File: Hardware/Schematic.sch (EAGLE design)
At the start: 105 parts, among them IC1 BQ25180YBGR, IC2 DRV2605YZFR, IC3 BMA423, IC9 RT6160AWSC, J1 503480-2400, J2 TC2030-IDC, J4 KH-TYPE-C-16P, Q1 20V/4.2A/52mΩ/1.4W, Q3 SI1308EDL-T1-GE3, U1 NRF52840_QF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

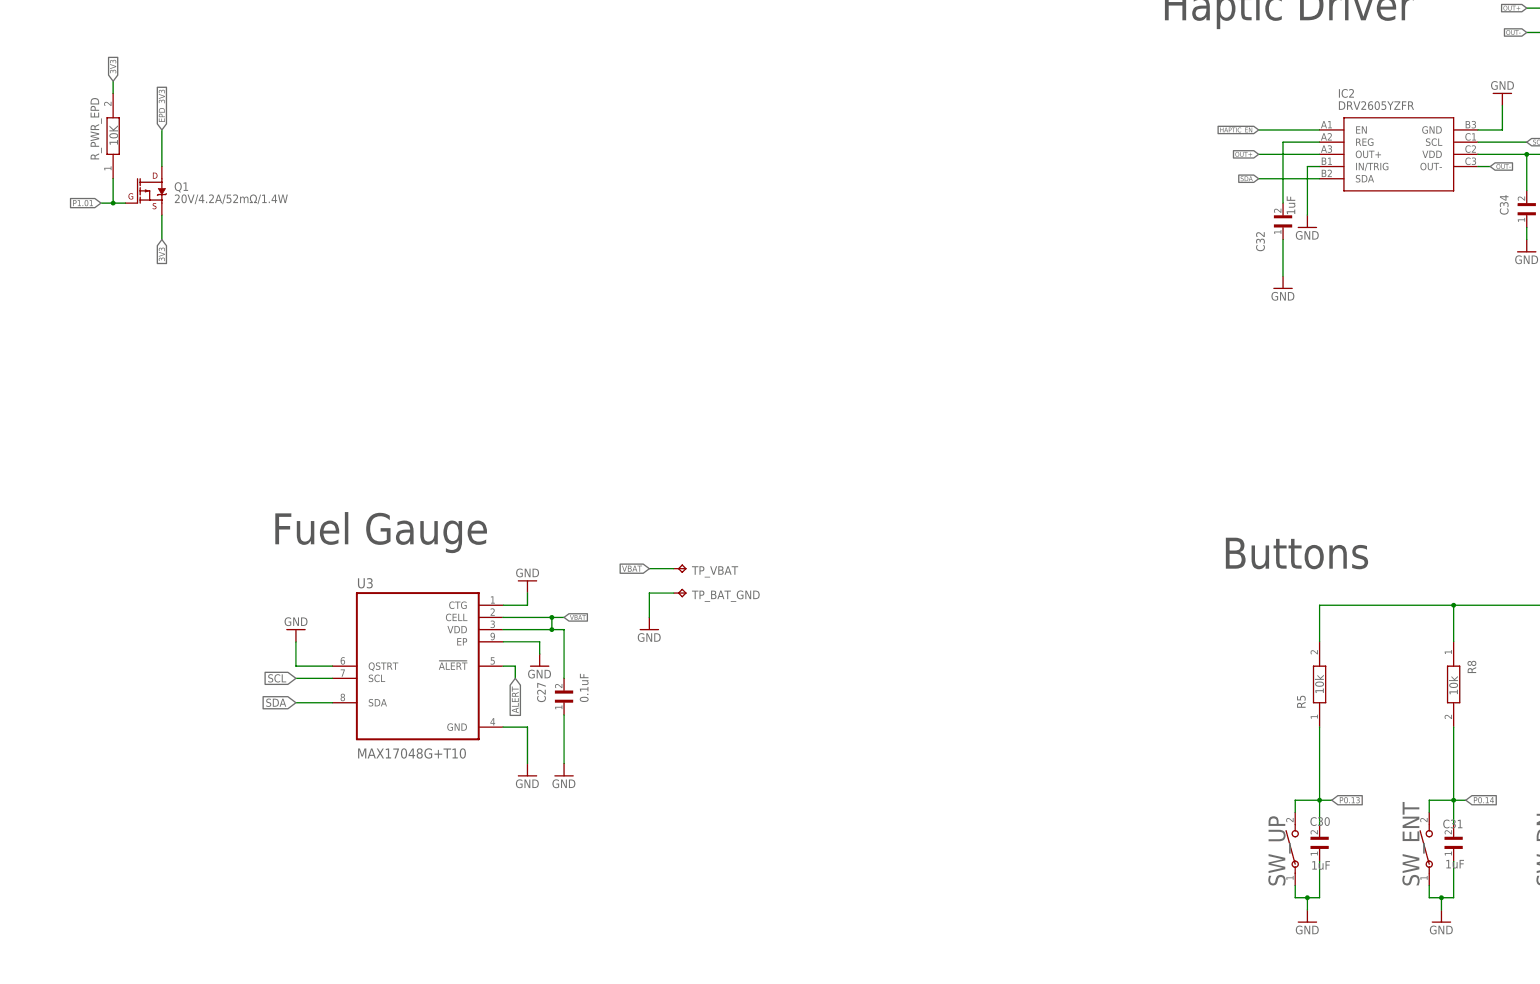
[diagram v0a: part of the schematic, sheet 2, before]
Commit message: Add 3D Models for all components
Added 3d Components for all PCB components along with different perspectives for the shell of the watch. Also fixed several issues with the layout.
Fixes #13
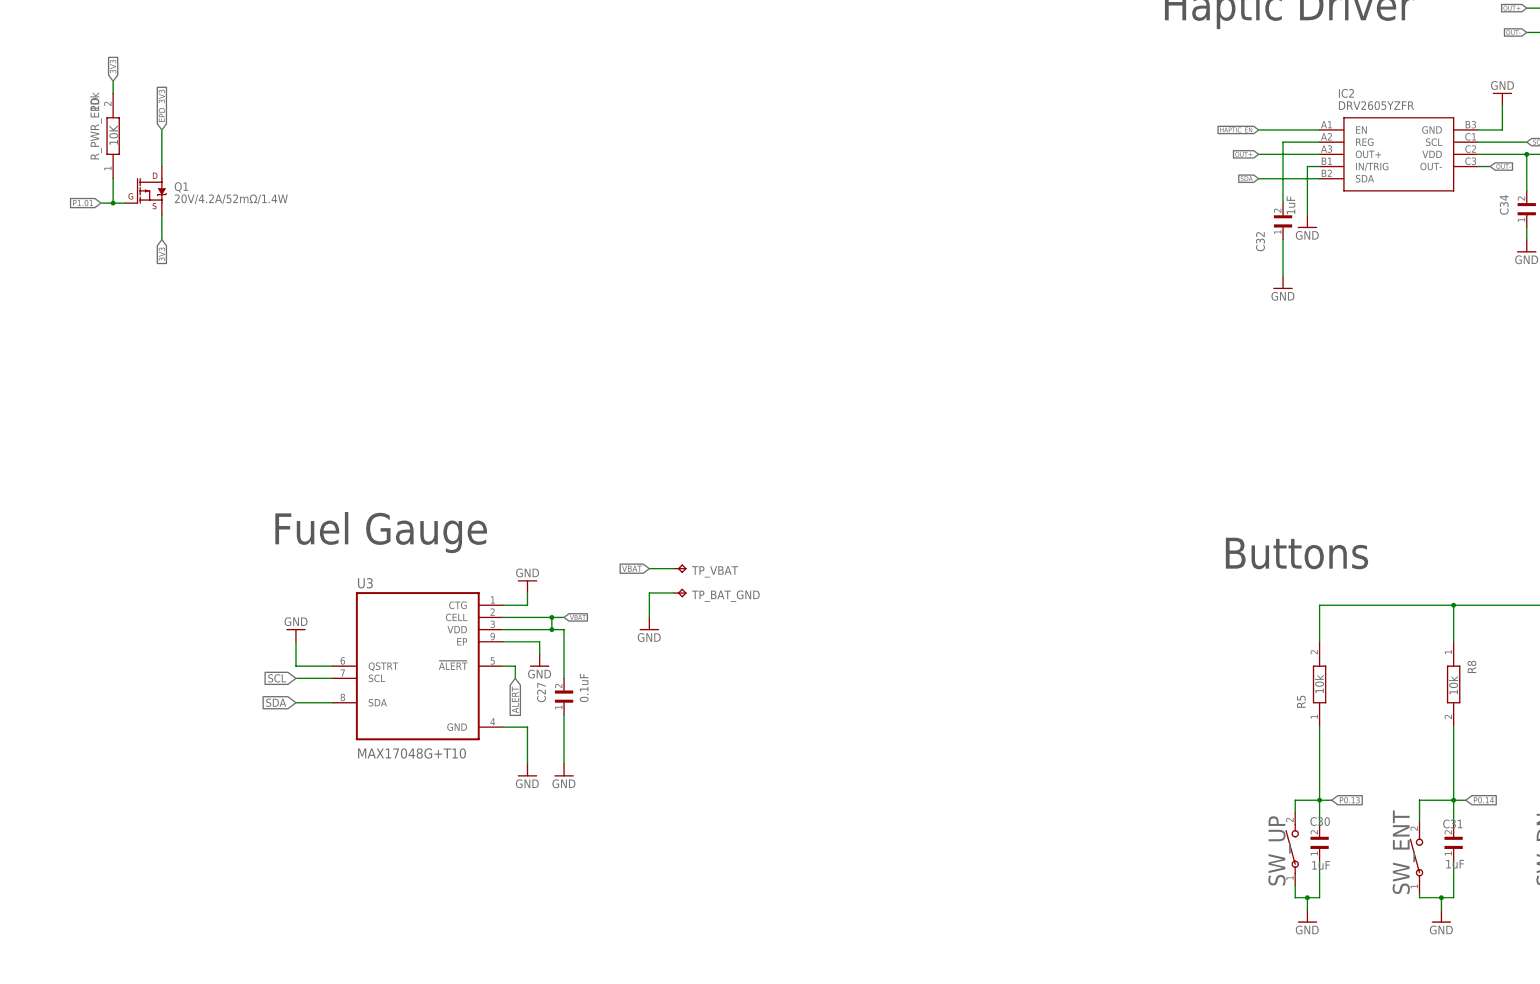
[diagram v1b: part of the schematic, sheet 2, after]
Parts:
- C25: device InkTime_v5:NORDIC_NRF_3_CAPACITOR_0402_L -> InkTime_v5:NORDIC_NRF_3_CAPACITOR_0201_L
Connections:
- removed net DEC4_6: L3.2
- removed net N$1: L2.1
- net N$32: now also L2.1
- net N$9: now also L3.2
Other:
- moved on the sheet: SW_ENT
